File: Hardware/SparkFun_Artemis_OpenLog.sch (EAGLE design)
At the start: 77 parts, among them J11 Qwiic, J14 CORTEX_JTAG, J17 MICRO-SD, Q1 20V/0.2A/8MHz/1.2Ω/1Vth, Q10 20V/0.2A/8MHz/1.2Ω/1Vth, Q3 20V/0.2A/8MHz/1.2Ω/1Vth, Q7 20V/0.2A/8MHz/1.2Ω/1Vth, Q9 20V/0.2A/8MHz/1.2Ω/1Vth, U10 CH340E, U13 ICM-20948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

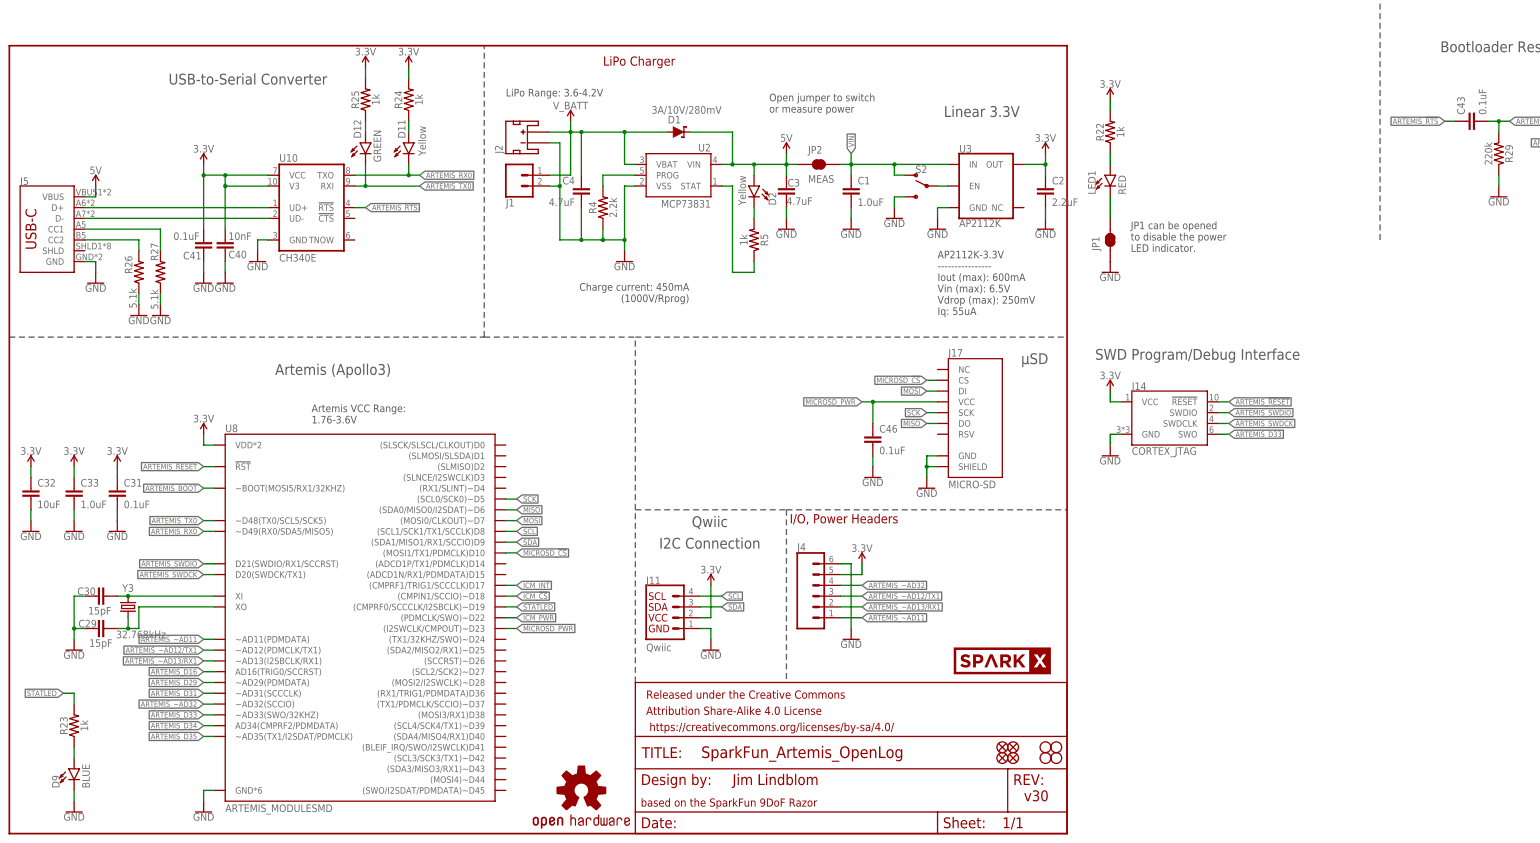
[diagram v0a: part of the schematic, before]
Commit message: Add RTC cap. Remove switch. Add Qwiic MOSFET.
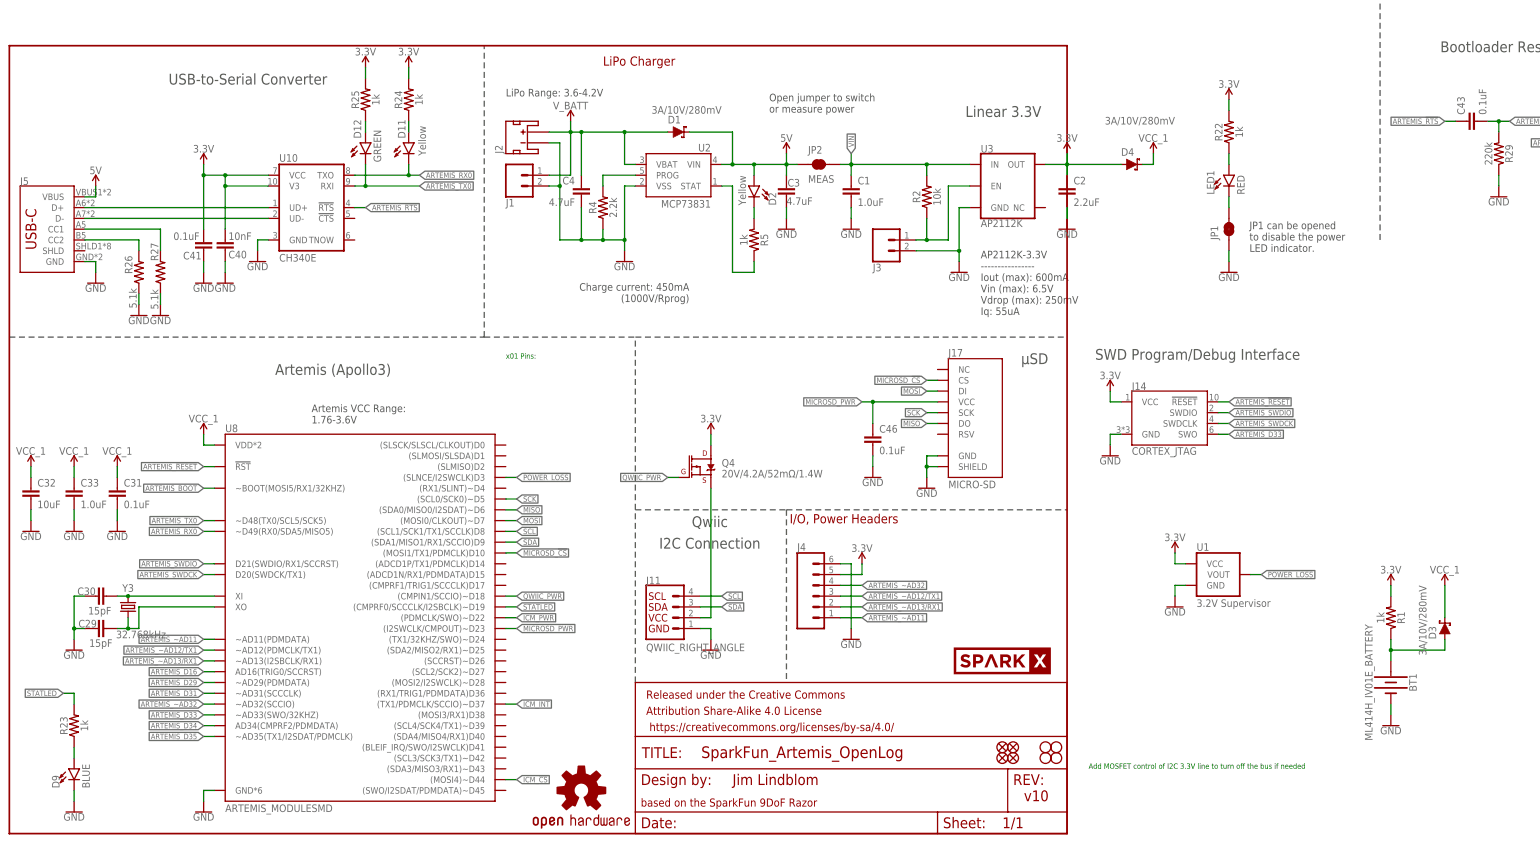
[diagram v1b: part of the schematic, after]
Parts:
- removed S2: (no value), SparkFun-Switches:SWITCH-SPDT-SMD-RIGHT-ANGLE
- added BT1: ML414H_IV01E_BATTERY, SparkFun-Batteries:ML414H_IV01E_BATTERY
- added D3, D4: 3A/10V/280mV, SparkFun-DiscreteSemi:DIODE-SCHOTTKY-BAT60A
- added J3: (no value), SparkFun-Connectors:CONN_021X02_NO_SILK
- added Q4: 20V/4.2A/52mΩ/1.4W, SparkFun-DiscreteSemi:MOSFET_PCH-DMG2305UX-7
- added R1: 1k, SparkFun-Resistors:1KOHM-0402T-1/16W-1%
- added R2: 10k, SparkFun-Resistors:10KOHM-0402T-1/16W-1%
- added U1: 3.2V Supervisor, SparkFun-IC-Power:V_SUPERVISOR
- J11: value Qwiic -> QWIIC_RIGHT_ANGLE
- U$6: value SPARKX-LOGO2 -> SPARKX-LOGO3; device SparkX:SPARKX-LOGO2 -> SparkX:SPARKX-LOGO3
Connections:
- new net !POWER_LOSS!: U1.VOUT, U8.(SLNCE/I2SWCLK)D3
- new net N$1: BT1.+, D3.A, R1.1
- new net QWIIC_PWR: Q4.G, U8.(CMPIN1/SCCIO)~D18
- new net VCC_1: C31.2, C32.1, C33.1, D3.C, D4.C, U8.VDD*2
- new net VREG_EN: J3.1, R2.1, U3.EN
- net 3.3V: now also D4.A, Q4.D, R1.2, U1.VCC; no longer C31.2, C32.1, C33.1, J11.2, U8.VDD*2
- net GND: now also BT1.-, J3.2, U1.GND; no longer S2.S
- net ICM_!CS!: now also U8.(MOSI4)~D44; no longer U8.(CMPIN1/SCCIO)~D18
- net ICM_INT: now also U8.(TX1/PDMCLK/SCCIO)~D37; no longer U8.(CMPRF1/TRIG1/SCCCLK)D17
- net N$5: now also J11.2, Q4.S; no longer S2.P, U3.EN
- net VIN: now also R2.2; no longer S2.O
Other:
- note added: "Add MOSFET control of I2C 3.3V line to turn off the bus if needed"
- note added: "v10"
- note added: "x01 Pins:"
- note removed: "v30"
- moved on the sheet: C2, JP1, LED1, R22, U3

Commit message: Add panel files.
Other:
- note added: "ICM_CS: 18"
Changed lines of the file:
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@@
 <grid distance="0.1" unitdist="inch" unit="inch" style="lines" multiple="1" display="no" altdistance="0.01" altunitdist="inch" altunit="inch"/>
 <layers>
-<layer number="1" name="Top" color="4" fill="1" visible="yes" active="no"/>
-<layer number="2" name="Route2" color="1" fill="3" visible="yes" active="no"/>
-<layer number="3" name="Route3" color="4" fill="3" visible="yes" active="no"/>
-<layer number="4" name="Route4" color="1" fill="4" visible="yes" active="no"/>
-<layer number="5" name="Route5" color="4" fill="4" visible="yes" active="no"/>
-<layer number="6" name="Route6" color="1" fill="8" visible="yes" active="no"/>
-<layer number="7" name="Route7" color="4" fill="8" visible="yes" active="no"/>
-<layer number="8" name="Route8" color="1" fill="2" visible="yes" active="no"/>
-<layer number="9" name="Route9" color="4" fill="2" visible="yes" active="no"/>
-<layer number="10" name="Route10" color="1" fill="7" visible="yes" active="no"/>
-<layer number="11" name="Route11" color="4" fill="7" visible="yes" active="no"/>
-<layer number="12" name="Route12" color="1" fill="5" visible="yes" active="no"/>
-<layer number="13" name="Route13" color="4" fill="5" visible="yes" active="no"/>
-<layer number="14" name="Route14" color="1" fill="6" visible="yes" active="no"/>
-<layer number="15" name="Route15" color="4" fill="6" visible="yes" active="no"/>
-<layer number="16" name="Bottom" color="1" fill="1" visible="yes" active="no"/>
-<layer number="17" name="Pads" color="2" fill="1" visible="yes" active="no"/>
-<layer number="18" name="Vias" color="2" fill="1" visible="yes" active="no"/>
-<layer number="19" name="Unrouted" color="6" fill="1" visible="yes" active="no"/>
-<layer number="20" name="Dimension" color="24" fill="1" visible="yes" active="no"/>
-<layer number="21" name="tPlace" color="16" fill="1" visible="yes" active="no"/>
-<layer number="22" name="bPlace" color="14" fill="1" visible="yes" active="no"/>
-<layer number="23" name="tOrigins" color="15" fill="1" visible="yes" active="no"/>
-<layer number="24" name="bOrigins" color="15" fill="1" visible="yes" active="no"/>
-<layer number="25" name="tNames" color="7" fill="1" visible="yes" active="no"/>
-<layer number="26" name="bNames" color="7" fill="1" visible="yes" active="no"/>
-<layer number="27" name="tValues" color="7" fill="1" visible="yes" active="no"/>
-<layer number="28" name="bValues" color="7" fill="1" visible="yes" active="no"/>
+<layer number="1" name="Top" color="4" fill="1" visible="no" active="no"/>
+<layer number="2" name="Route2" color="1" fill="3" visible="no" active="no"/>
+<layer number="3" name="Route3" color="4" fill="3" visible="no" active="no"/>
+<layer number="4" name="Route4" color="1" fill="4" visible="no" active="no"/>
+<layer number="5" name="Route5" color="4" fill="4" visible="no" active="no"/>
+<layer number="6" name="Route6" color="1" fill="8" visible="no" active="no"/>
+<layer number="7" name="Route7" color="4" fill="8" visible="no" active="no"/>
+<layer number="8" name="Route8" color="1" fill="2" visible="no" active="no"/>
+<layer number="9" name="Route9" color="4" fill="2" visible="no" active="no"/>
+<layer number="10" name="Route10" color="1" fill="7" visible="no" active="no"/>
+<layer number="11" name="Route11" color="4" fill="7" visible="no" active="no"/>
+<layer number="12" name="Route12" color="1" fill="5" visible="no" active="no"/>
+<layer number="13" name="Route13" color="4" fill="5" visible="no" active="no"/>
+<layer number="14" name="Route14" color="1" fill="6" visible="no" active="no"/>
+<layer number="15" name="Route15" color="4" fill="6" visible="no" active="no"/>
+<layer number="16" name="Bottom" color="1" fill="1" visible="no" active="no"/>
+<layer number="17" name="Pads" color="2" fill="1" visible="no" active="no"/>
+<layer number="18" name="Vias" color="2" fill="1" visible="no" active="no"/>
+<layer number="19" name="Unrouted" color="6" fill="1" visible="no" active="no"/>
+<layer number="20" name="Dimension" color="24" fill="1" visible="no" active="no"/>
+<layer number="21" name="tPlace" color="16" fill="1" visible="no" active="no"/>
+<layer number="22" name="bPlace" color="14" fill="1" visible="no" active="no"/>
+<layer number="23" name="tOrigins" color="15" fill="1" visible="no" active="no"/>
+<layer number="24" name="bOrigins" color="15" fill="1" visible="no" active="no"/>
+<layer number="25" name="tNames" color="7" fill="1" visible="no" active="no"/>
+<layer number="26" name="bNames" color="7" fill="1" visible="no" active="no"/>
+<layer number="27" name="tValues" color="7" fill="1" visible="no" active="no"/>
+<layer number="28" name="bValues" color="7" fill="1" visible="no" active="no"/>
 <layer number="29" name="tStop" color="7" fill="3" visible="no" active="no"/>
 <layer number="30" name="bStop" color="7" fill="6" visible="no" active="no"/>
@@
 <layer number="35" name="tGlue" color="7" fill="4" visible="no" active="no"/>
 <layer number="36" name="bGlue" color="7" fill="5" visible="no" active="no"/>
-<layer number="37" name="tTest" color="7" fill="1" visible="yes" active="no"/>
-<layer number="38" name="bTest" color="7" fill="1" visible="yes" active="no"/>
+<layer number="37" name="tTest" color="7" fill="1" visible="no" active="no"/>
+<layer number="38" name="bTest" color="7" fill="1" visible="no" active="no"/>
 <layer number="39" name="tKeepout" color="4" fill="11" visible="no" active="no"/>
 <layer number="40" name="bKeepout" color="1" fill="11" visible="no" active="no"/>
@@
 <layer number="44" name="Drills" color="7" fill="1" visible="no" active="no"/>
 <layer number="45" name="Holes" color="7" fill="1" visible="no" active="no"/>
-<layer number="46" name="Milling" color="3" fill="1" visible="yes" active="no"/>
-<layer number="47" name="Measures" color="7" fill="1" visible="yes" active="no"/>
-<layer number="48" name="Document" color="7" fill="1" visible="yes" active="no"/>
-<layer number="49" name="Reference" color="7" fill="1" visible="yes" active="no"/>
-<layer number="50" name="dxf" color="7" fill="1" visible="yes" active="no"/>
-<layer number="51" name="tDocu" color="6" fill="1" visible="yes" active="no"/>
-<layer number="52" name="bDocu" color="7" fill="1" visible="yes" active="no"/>
-<layer number="53" name="tGND_GNDA" color="7" fill="9" visible="yes" active="no"/>
-<layer number="54" name="bGND_GNDA" color="1" fill="9" visible="yes" active="no"/>
-<layer number="56" name="wert" color="7" fill="1" visible="yes" active="no"/>
-<layer number="57" name="tCAD" color="7" fill="1" visible="yes" active="no"/>
-<layer number="59" name="tCarbon" color="7" fill="1" visible="yes" active="no"/>
-<layer number="60" name="bCarbon" color="7" fill="1" visible="yes" active="no"/>
+<layer number="46" name="Milling" color="3" fill="1" visible="no" active="no"/>
+<layer number="47" name="Measures" color="7" fill="1" visible="no" active="no"/>
+<layer number="48" name="Document" color="7" fill="1" visible="no" active="no"/>
+<layer number="49" name="Reference" color="7" fill="1" visible="no" active="no"/>
+<layer number="50" name="dxf" color="7" fill="1" visible="no" active="no"/>
+<layer number="51" name="tDocu" color="6" fill="1" visible="no" active="no"/>
+<layer number="52" name="bDocu" color="7" fill="1" visible="no" active="no"/>
+<layer number="53" name="tGND_GNDA" color="7" fill="9" visible="no" active="no"/>
+<layer number="54" name="bGND_GNDA" color="1" fill="9" visible="no" active="no"/>
+<layer number="56" name="wert" color="7" fill="1" visible="no" active="no"/>
+<layer number="57" name="tCAD" color="7" fill="1" visible="no" active="no"/>
+<layer number="59" name="tCarbon" color="7" fill="1" visible="no" active="no"/>
+<layer number="60" name="bCarbon" color="7" fill="1" visible="no" active="no"/>
 <layer number="88" name="SimResults" color="9" fill="1" visible="no" active="no"/>
 <layer number="89" name="SimProbes" color="9" fill="1" visible="no" active="no"/>
@@
 <text x="254" y="15.24" size="1.27" layer="91">Add MOSFET control of I2C 3.3V line to turn off the bus if needed</text>
 <text x="116.84" y="111.76" size="1.27" layer="91">x01 Pins:</text>
+<text x="119.38" y="109.22" size="1.27" layer="91">ICM_CS: 18</text>
+<text x="119.38" y="106.68" size="1.27" layer="91">ICM_CS: 18</text>
 </plain>
 <instances>

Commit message: Change RTC battery charging circuit. Fix PNP Qwiic MOSFET.
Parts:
- removed D4: 3A/10V/280mV, SparkFun-DiscreteSemi:DIODE-SCHOTTKY-BAT60A
- added C5: 10uF, SparkFun-Capacitors:10UF-0603-6.3V-20%
- added C6: 1.0uF, SparkFun-Capacitors:1.0UF-0402T-16V-10%
- added D6: 1A/23V/620mV, SparkFun-DiscreteSemi:DIODE-SCHOTTKY-BAT20J
- BT1: value ML414H_IV01E_BATTERY -> ML414H
- C29, C30: device SparkFun-Capacitors:15PF-0402-50V-5% -> SparkFun-Capacitors:15PF-0402T-50V-5%
- FRAME1: value FRAME-LETTER -> FRAME-LEDGER; device SparkFun-Aesthetics:FRAME-LETTER -> SparkFun-Aesthetics:FRAME-LEDGER
- J11: value QWIIC_RIGHT_ANGLE -> (none)
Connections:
- net 3.3V: now also C5.1, C6.1, D6.A, Q4.S; no longer D4.A, Q4.D, R1.2, R28.2
- net GND: now also C5.2, C6.2
- net N$5: now also Q4.D; no longer Q4.S
- net VCC_1: now also D6.C, R1.2, R28.2; no longer D4.C
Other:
- note added: "0.65uA / 0.3V drop at 10mA"
- note added: "300uA"
- note added: "Based on the SparkFun 9DoF Razor"
- note added: "N. Seidle"
- note added: "Optional External Switch"
- note added: "RTC Battery"
- note added: "x02"
- note removed: "Add MOSFET control of I2C 3.3V line to turn off the bus if needed"
- note removed: "I2C Connection"
- note removed: "Jim Lindblom"
- note removed: "based on the SparkFun 9DoF Razor"
- note removed: "v10"
- moved on the sheet: BT1, C1, C2, C29, C3, C30, C31, C32, C33, C4, C40, C41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
